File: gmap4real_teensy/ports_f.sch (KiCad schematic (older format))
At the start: 6 parts

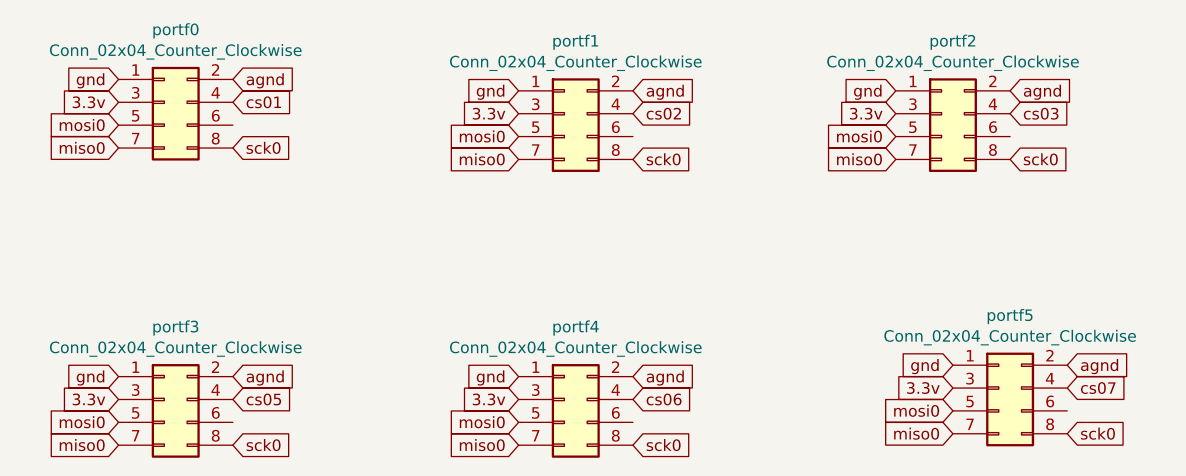
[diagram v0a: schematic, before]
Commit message: teensy: fix select pin conflict
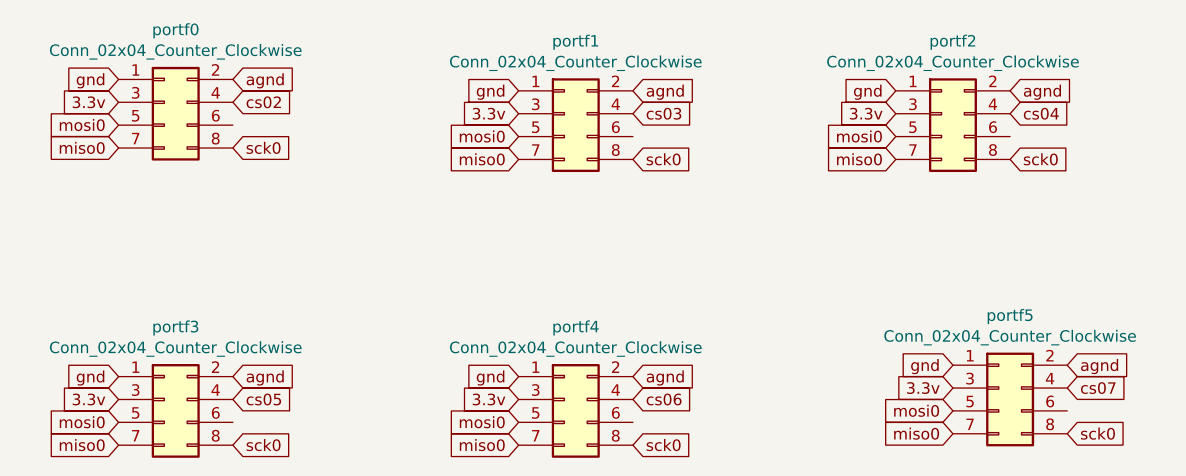
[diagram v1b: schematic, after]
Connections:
- net cs01 is gone; now on net cs02: portf0.4 (Pin_4)
- net cs02: no longer portf1.4 (Pin_4)
- net cs03: now also portf1.4 (Pin_4); no longer portf2.4 (Pin_4)
- new net cs04: portf2.4 (Pin_4)
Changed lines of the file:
@@
 sck0
 Text GLabel 2200 1700 2    50   Input ~ 0
-cs01
+cs02
 Text GLabel 2200 1600 2    50   Input ~ 0
 agnd
@@
 sck0
 Text GLabel 3950 1750 2    50   Input ~ 0
-cs02
+cs03
 Text GLabel 3950 1650 2    50   Input ~ 0
 agnd
@@
 sck0
 Text GLabel 5600 1750 2    50   Input ~ 0
-cs03
+cs04
 Text GLabel 5600 1650 2    50   Input ~ 0
 agnd
